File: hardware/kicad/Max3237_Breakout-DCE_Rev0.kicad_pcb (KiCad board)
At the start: 2 copper layers, 31.8 x 51.4 mm, 13 parts, among them J1 TTL_HEADER, J2 DE9_RS232, J3 MBAUD, J4 ENABLE, J5 SHUTDOWN, U1 MAX3237EIPWR

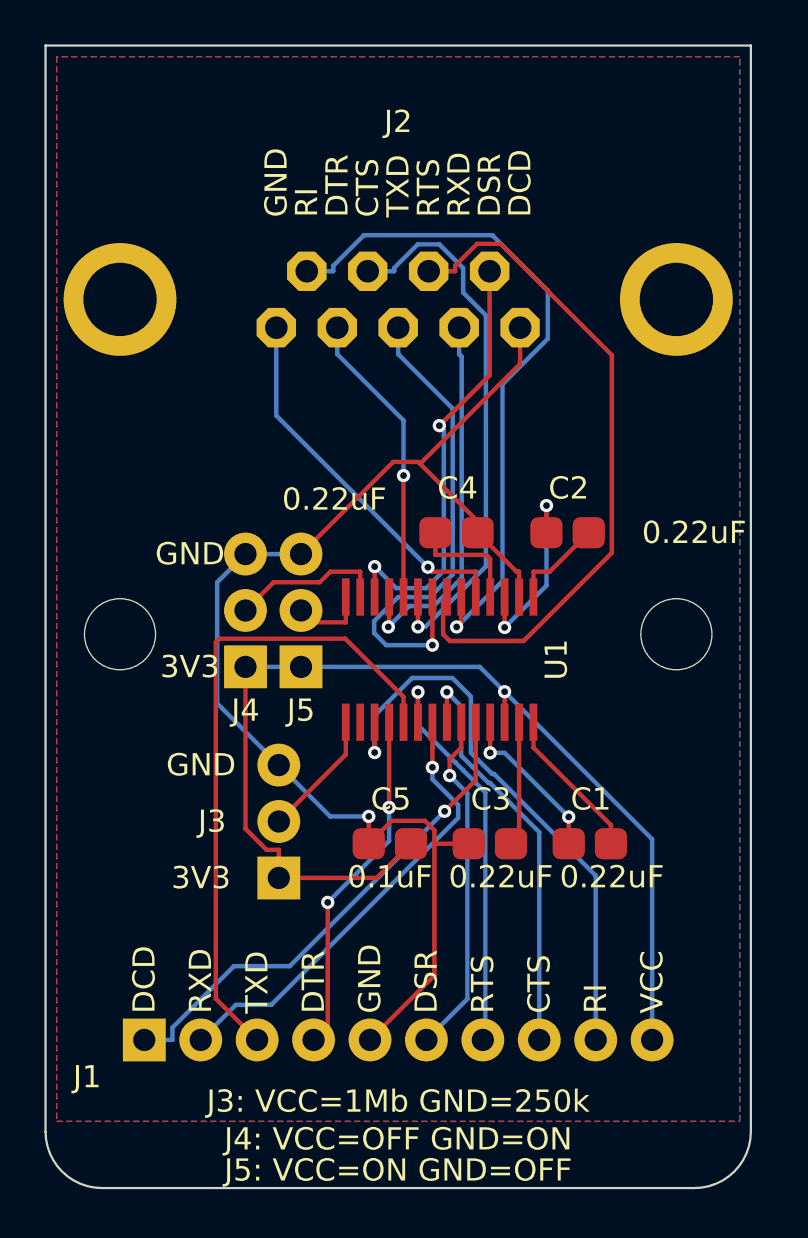
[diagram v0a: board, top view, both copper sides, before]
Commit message: Full rip/reroute/repour; add Power net class for a wider +3.3V trace
Freerouting's fanout-via placement was scattering the mandatory
0.5mm pour clearance halos somewhat differently on each reroute,
which read as odd curved voids/slivers in the pour in a few spots
(most visibly near C4). No DRC violation, but genuinely inconsistent
with a hand-tuned layout. Ripped all copper and re-routed/re-poured
from scratch (Freerouting, single-threaded, 100 passes, global
strategy - same settings as before) rather than chase individual
via placements.

Also added a dedicated "Power" net class (0.4mm track width, vs the
0.2mm Default) and assigned +3.3V to it, so the VCC rail routes
noticeably wider than signal traces. Verified via the DSN export that
Freerouting picked up the 400um width rule before routing, rather
than just widening the result after the fact.

Two GND pads (J2 pad 5, J1 pad 5) came up short on thermal-relief
spoke count on this route and were set to a solid zone connection,
same fix as the previous starved-thermal cleanup.

DRC: 0 unconnected, 0 violations beyond the pre-existing, unrelated
footprint-library-path warnings.

Co-Authored-By: Claude Sonnet 5 <noreply@anthropic.com>
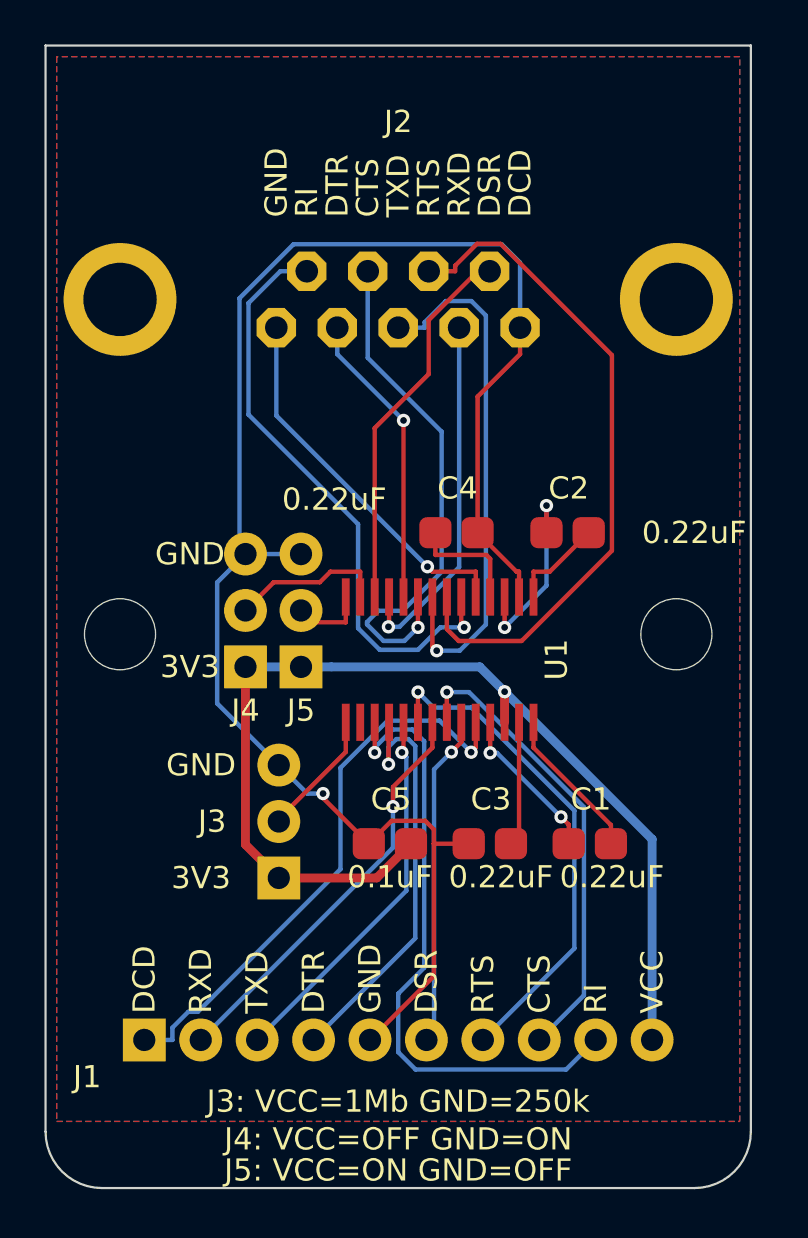
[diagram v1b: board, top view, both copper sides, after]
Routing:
- net GND: track 58.7 -> 77.3 mm
- net /TTL-TXD: track 29.4 -> 17.2 mm, vias 0 -> 1
- net /TTL-RTS: track 18.3 -> 22.6 mm
- net /RS232-DSR: track 31.0 -> 26.9 mm
- net /TTL-DTR: track 15.7 -> 19.3 mm, vias 2 -> 1
- net /TTL-DCD: track 22.7 -> 25.7 mm
- net /RS232-RI: track 19.7 -> 17.1 mm, vias 2 -> 0
- net /TTL-RI: track 26.2 -> 28.6 mm
- net /TTL-CTS: track 18.8 -> 21.0 mm
- net /TTL-RXD: track 20.5 -> 18.6 mm
- net /RS232-TXD: track 22.1 -> 24.0 mm
- net /RS232-RTS: track 24.7 -> 23.5 mm
- net /TTL-DSR: track 15.6 -> 15.0 mm
